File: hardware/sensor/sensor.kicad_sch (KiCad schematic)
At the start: 1 part, among them IC1 ATTINY202-SSN

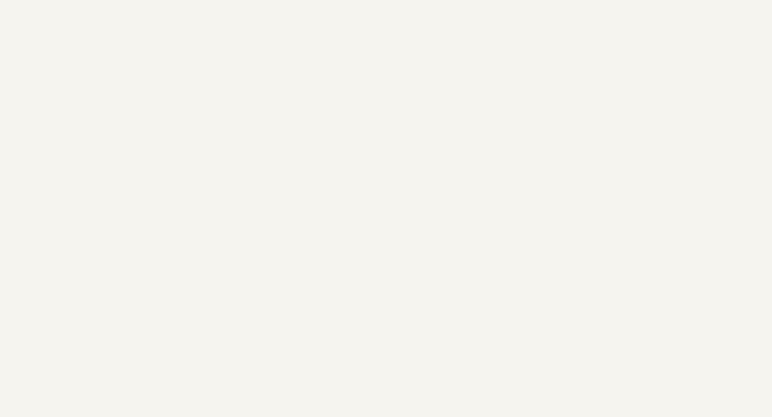
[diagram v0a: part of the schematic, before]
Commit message: EG-21 Added datasheets and the main ICs to KiCad project library, including symbol, footprint and 3D model.
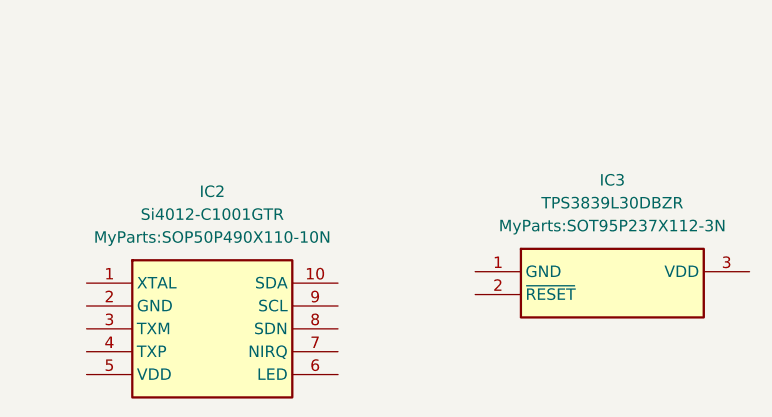
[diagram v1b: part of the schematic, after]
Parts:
- added IC2: Si4012-C1001GTR, MyParts:SOP50P490X110-10N, symbol Si4012-C1001GTR:Si4012-C1001GTR
- added IC3: TPS3839L30DBZR, MyParts:SOT95P237X112-3N, symbol TPS3839L30DBZR:TPS3839L30DBZR

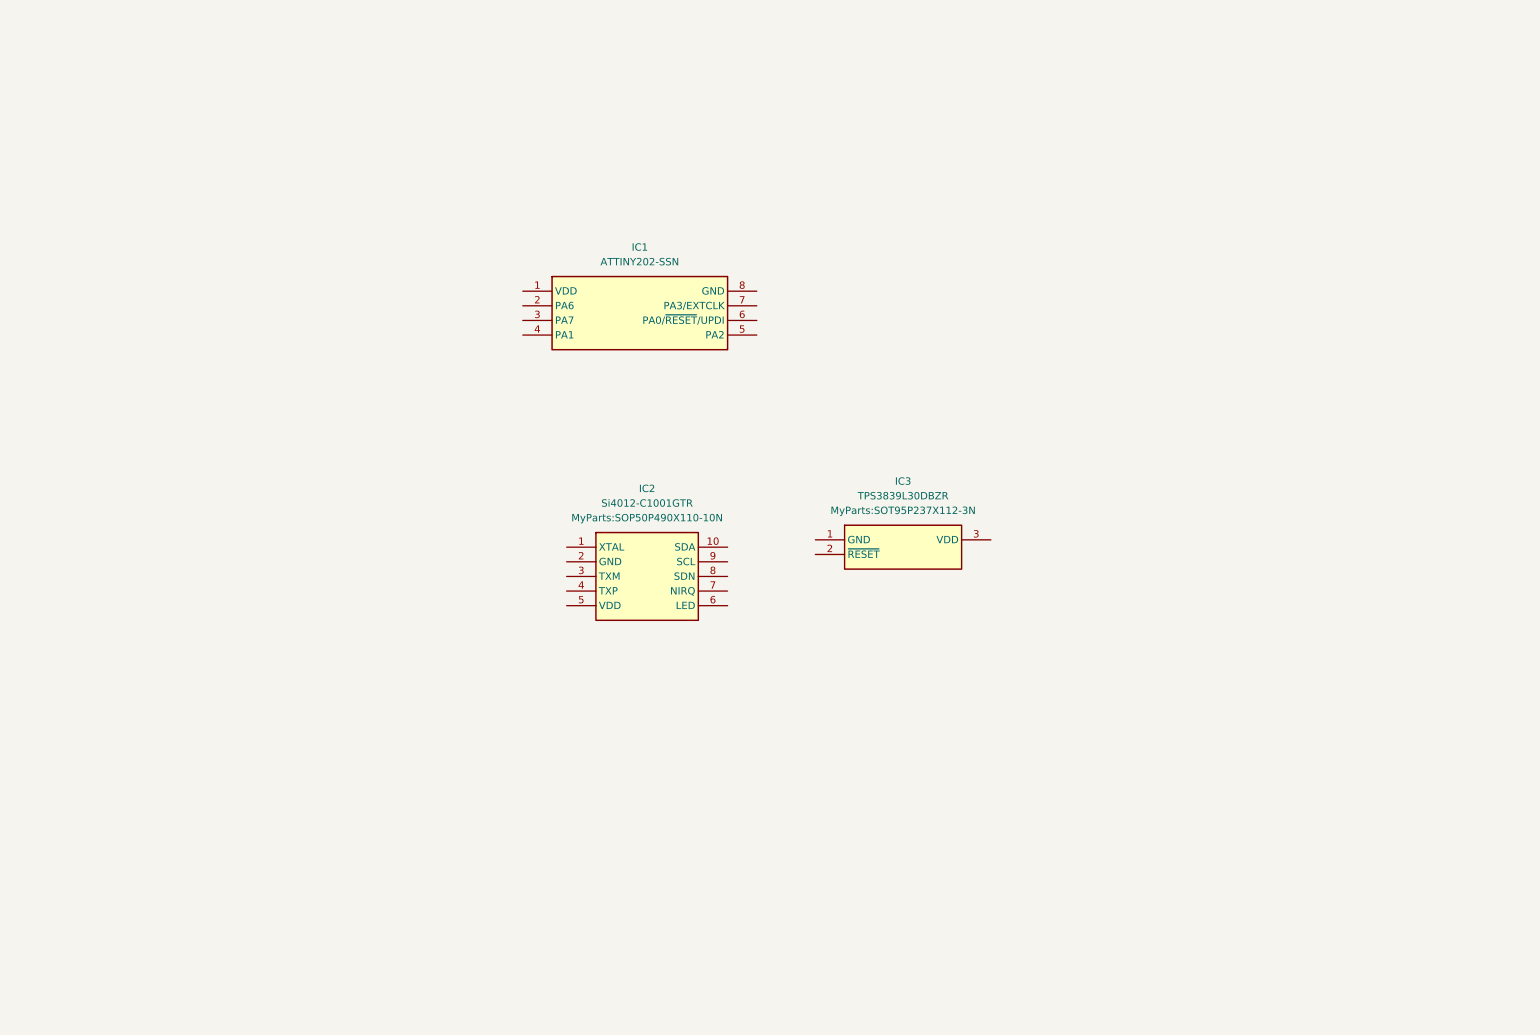
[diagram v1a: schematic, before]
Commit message: EG-21 Main components on schematic. Only missing I2C resistors, antenna, MCU RESET signal handling  and signals MCU<->Si4012.
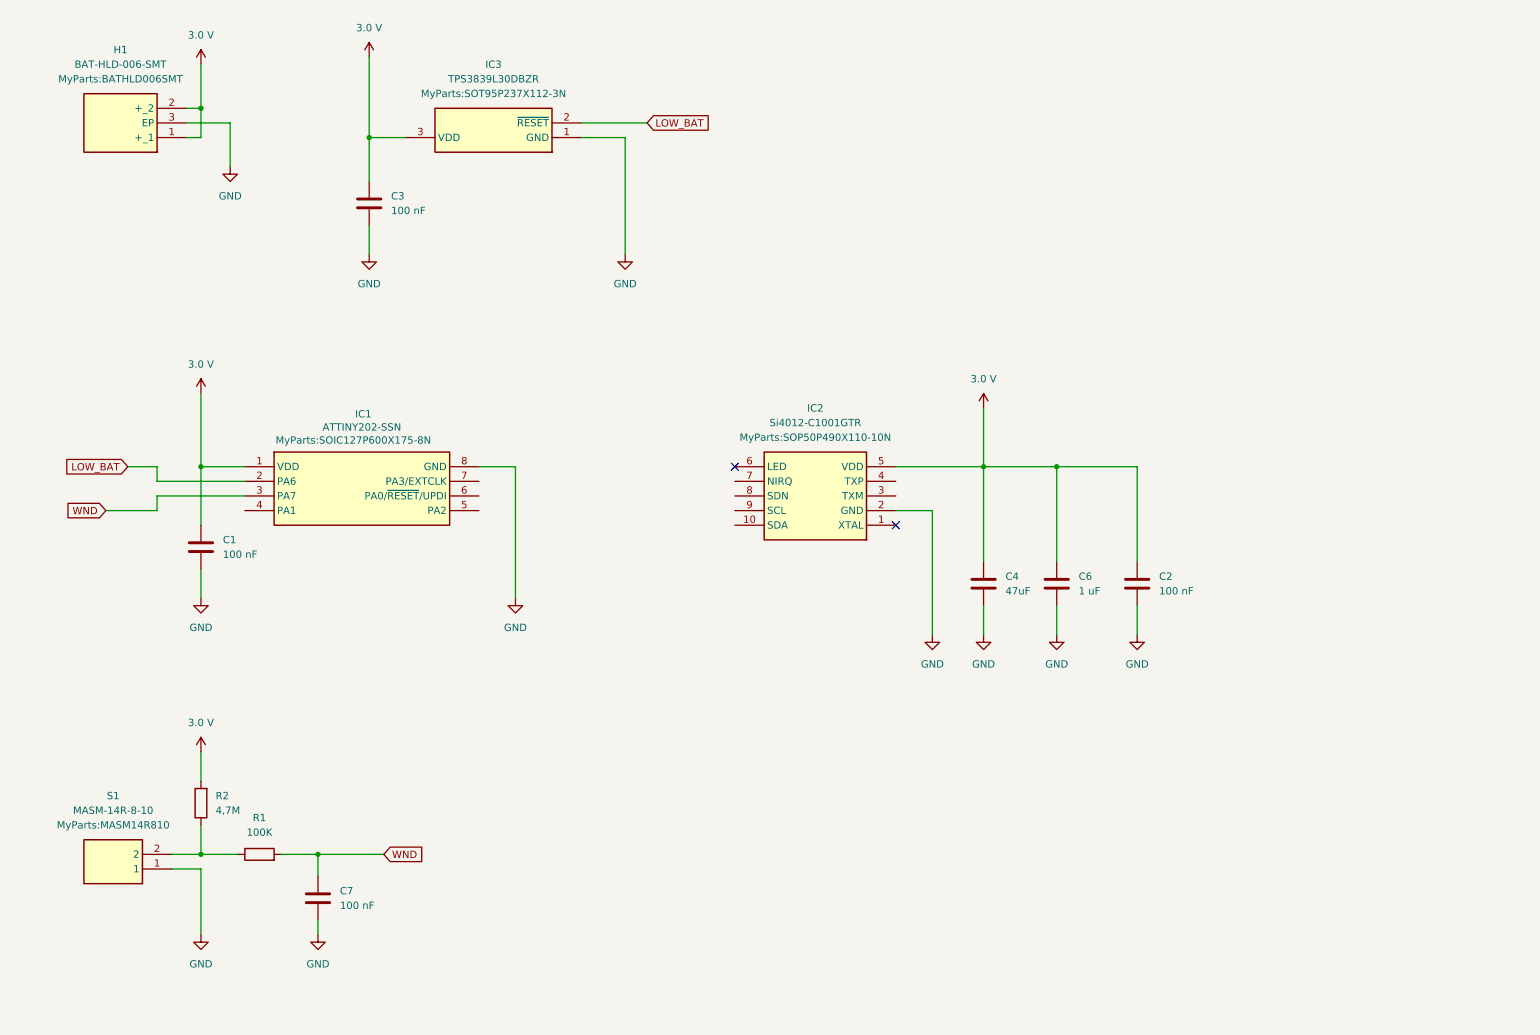
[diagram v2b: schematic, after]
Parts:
- added C1, C2, C3, C7: 100 nF, Capacitor_SMD:C_0603_1608Metric, symbol Device:C
- added C4: 47uF, symbol Device:C
- added C6: 1 uF, Capacitor_SMD:C_0603_1608Metric, symbol Device:C
- added H1: BAT-HLD-006-SMT, MyParts:BATHLD006SMT, symbol BAT-HLD-006-SMT:BAT-HLD-006-SMT
- added R1: 100K, Resistor_SMD:R_0201_0603Metric, symbol Device:R
- added R2: 4,7M, symbol Device:R
- added S1: MASM-14R-8-10, MyParts:MASM14R810, symbol MASM-14R-8-10:MASM-14R-8-10
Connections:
- net 3.0 V: now reaches IC1.1 (VDD)
- net 3.0 V: now also IC2.5 (VDD), IC3.3 (VDD), C1.1, C2.1, C3.1, C4.1, C6.1, H1.1 (+_1), H1.2 (+_2), R2.2
- net LOW_BAT: now reaches IC1.2 (PA6)
- net LOW_BAT: now also IC3.2 (~{RESET})
- net WND: now reaches IC1.3 (PA7)
- net WND: now also C7.1, R1.2
- net GND: now reaches IC1.8 (GND)
- net GND: now also IC2.2 (GND), IC3.1 (GND), C1.2, C2.2, C3.2, C4.2, C6.2, C7.2, H1.3 (EP), S1.1
- new net: R1.1, R2.1, S1.2
- no-connect marks 0 -> 2
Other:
- moved on the sheet: IC1, IC2, IC3

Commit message: EG-21 Added all components except the antenna balun and antenna footprint. Added the Si4012 antenna application note.
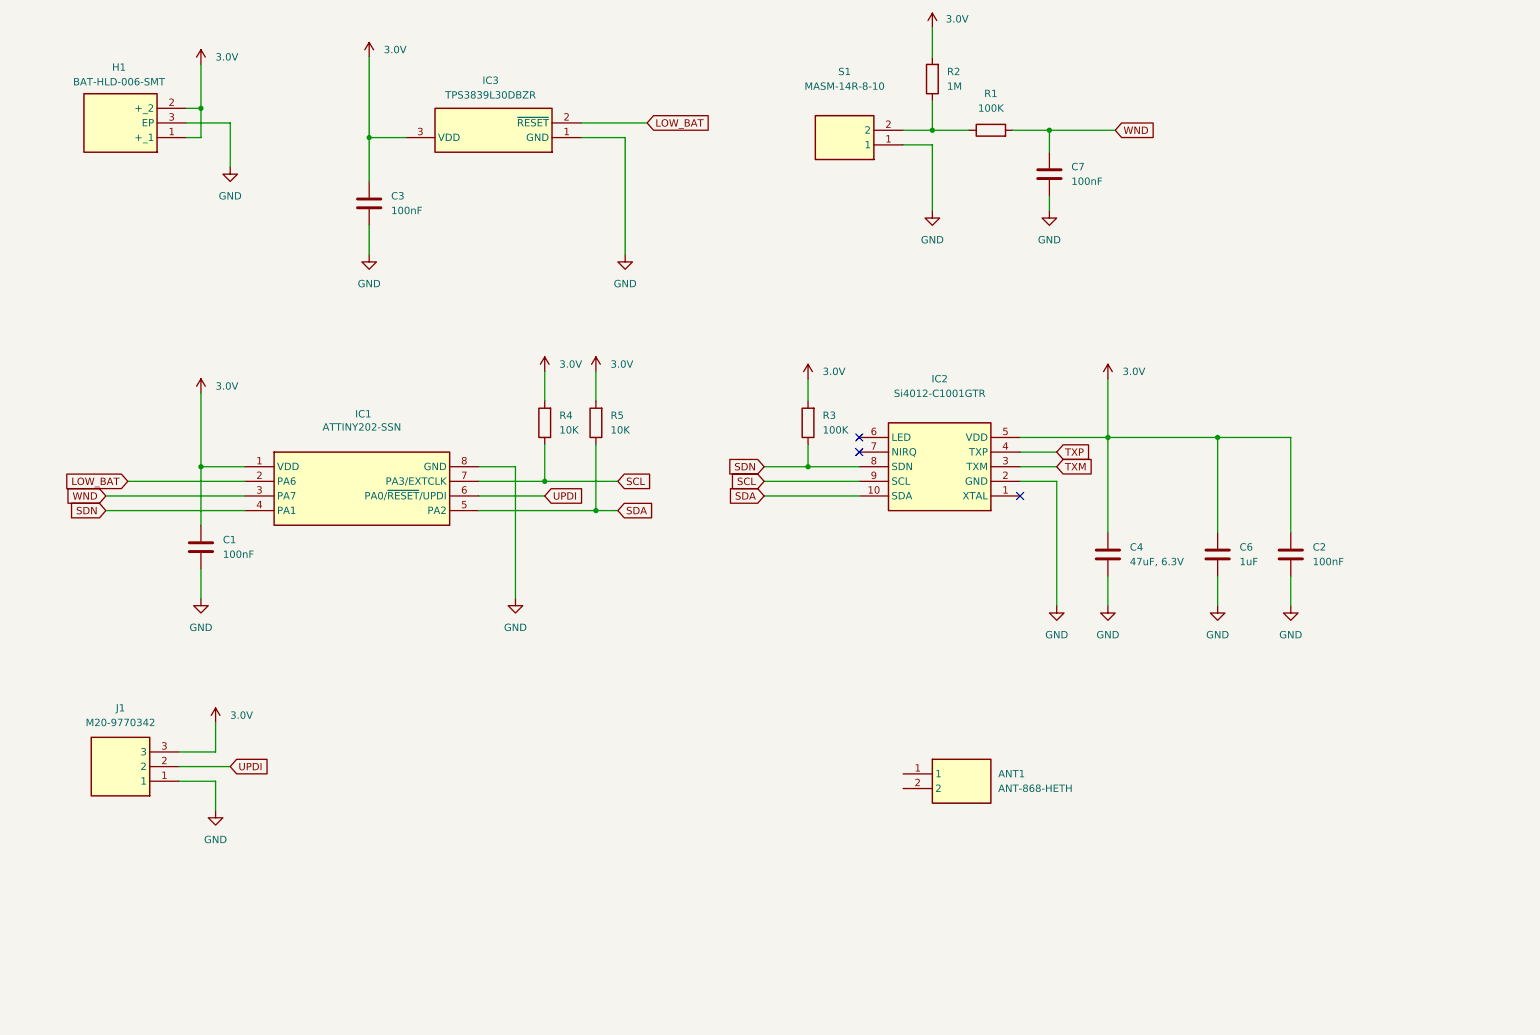
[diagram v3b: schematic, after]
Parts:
- added ANT1: ANT-868-HETH, ANT868HETH, symbol ANT-868-HESM:ANT-868-HETH
- added J1: M20-9770342, MyParts:HDRV3W66P0X254_1X3_762X254X855P, symbol M20-9770342:M20-9770342
- added R3: 100K, Resistor_SMD:R_0201_0603Metric, symbol Device:R
- added R4, R5: 10K, Resistor_SMD:R_0201_0603Metric, symbol Device:R
- C1, C2, C3, C7: value 100 nF -> 100nF
- C4: value 47uF -> 47uF, 6.3V; footprint (none) -> Capacitor_SMD:C_0805_2012Metric
- C6: value 1 uF -> 1uF
- R2: value 4,7M -> 1M
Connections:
- net GND: now also J1.1
- net SDN: now reaches IC1.4 (PA1)
- net SDN: now also IC2.8 (SDN), R3.1
- net SDA: now reaches IC1.5 (PA2)
- net SDA: now also IC2.10 (SDA), R5.1
- net UPDI: now reaches IC1.6 (PA0/~{RESET}/UPDI)
- net UPDI: now also J1.2
- net SCL: now reaches IC1.7 (PA3/EXTCLK)
- net SCL: now also IC2.9 (SCL), R4.1
- net TXM: now reaches IC2.3 (TXM)
- net TXP: now reaches IC2.4 (TXP)
- net 3.0 V renamed 3.0V
- net 3.0V: now also J1.3, R3.2, R4.2, R5.2
- no-connect marks 2 -> 3
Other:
- moved on the sheet: C2, C4, C6, C7, IC2, R1, R2, S1

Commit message: EG-21 Antenna and programming headers added. Missing the balun part and test points.
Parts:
- ANT1: footprint ANT868HETH -> MyParts:ANT-868-HESM
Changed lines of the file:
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@@
 			)
 		)
-		(property "Footprint" "ANT868HETH"
+		(property "Footprint" "MyParts:ANT-868-HESM"
 			(at 182.88 242.24 0)
 			(effects

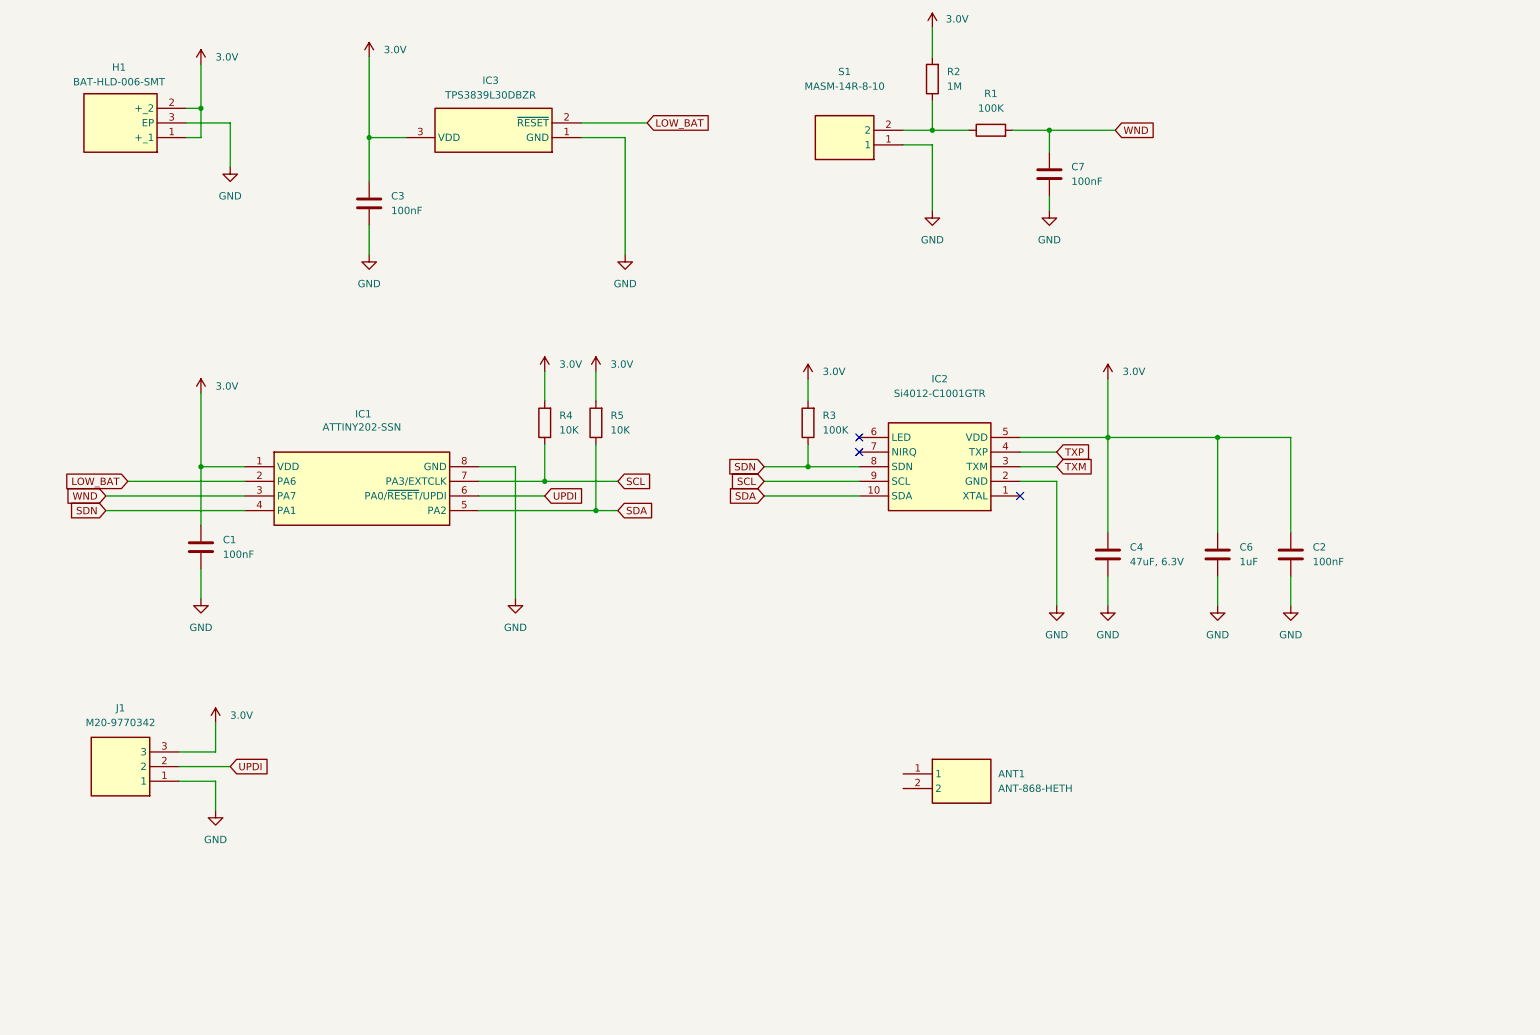
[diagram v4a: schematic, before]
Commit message: EG-21 Balun, pi-matching and antenna connected.
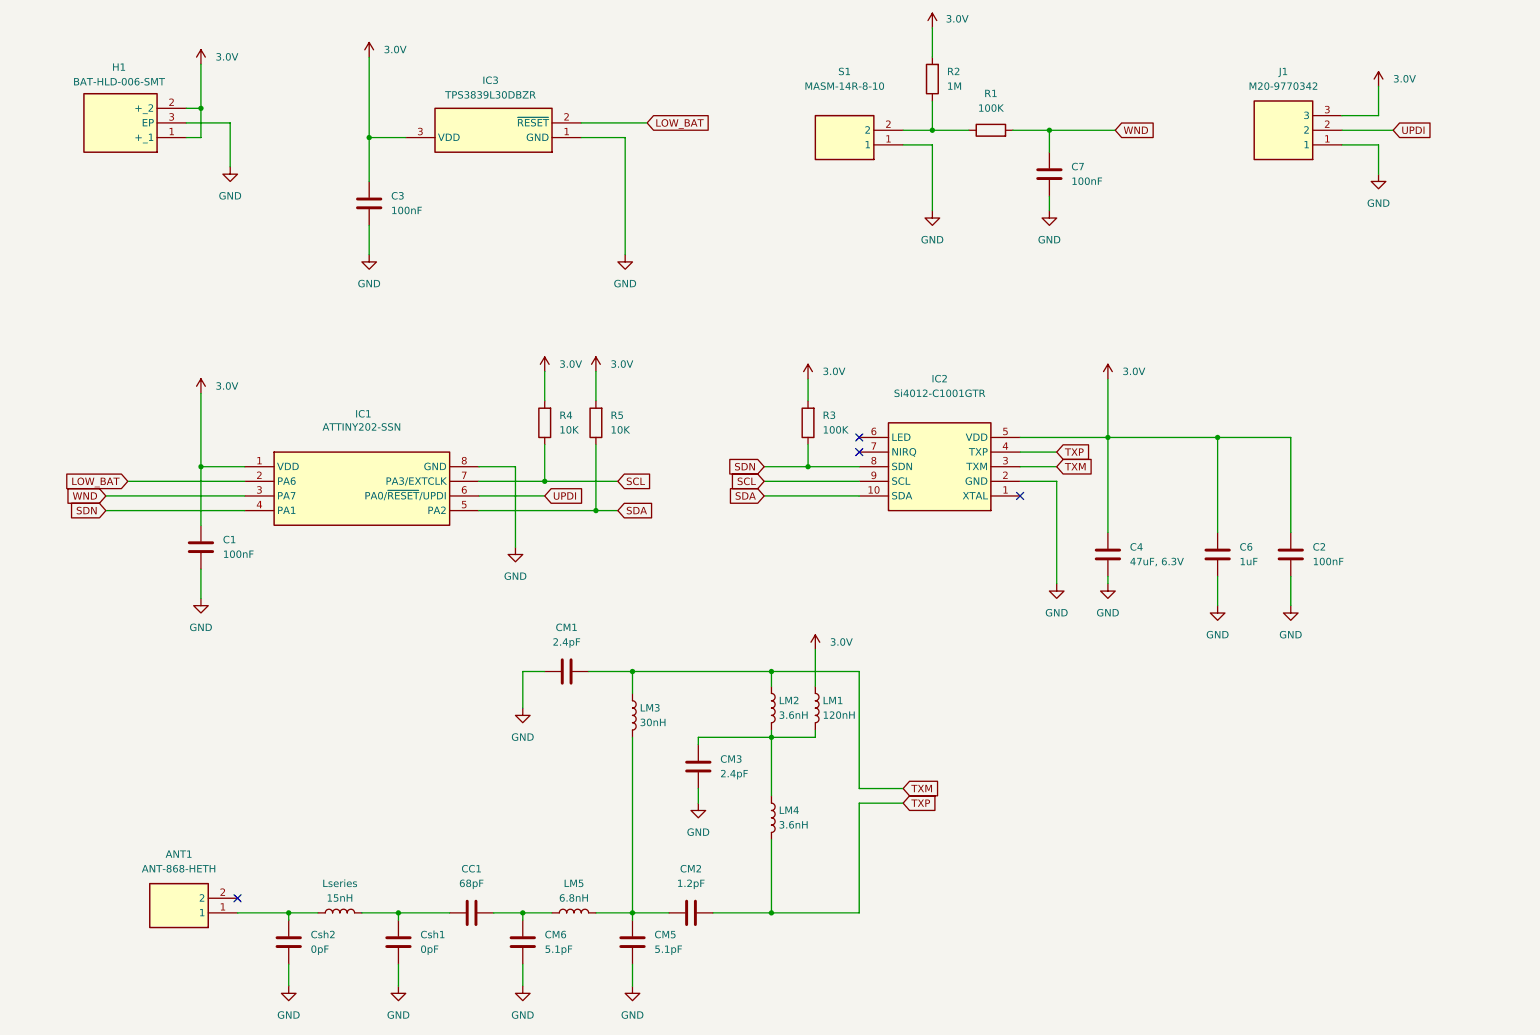
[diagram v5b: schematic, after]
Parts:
- added CC1: 68pF, Inductor_SMD:L_0402_1005Metric, symbol Device:C
- added CM1, CM3: 2.4pF, Inductor_SMD:L_0402_1005Metric, symbol Device:C
- added CM2: 1.2pF, Inductor_SMD:L_0402_1005Metric, symbol Device:C
- added CM5: 5.1pF, symbol Device:C
- added CM6: 5.1pF, Inductor_SMD:L_0402_1005Metric, symbol Device:C
- added Csh1, Csh2: 0pF, symbol Device:C
- added LM1: 120nH, Inductor_SMD:L_0603_1608Metric, symbol Device:L
- added LM2, LM4: 3.6nH, Inductor_SMD:L_0402_1005Metric, symbol Device:L
- added LM3: 30nH, Inductor_SMD:L_0402_1005Metric, symbol Device:L
- added LM5: 6.8nH, Inductor_SMD:L_0402_1005Metric, symbol Device:L
- added Lseries: 15nH, Inductor_SMD:L_0402_1005Metric, symbol Device:L
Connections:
- net 3.0V: now also LM1.1
- net GND: now also CM1.2, CM3.2, CM5.2, CM6.2, Csh1.2, Csh2.2
- net TXM: now also CM1.1, LM2.1, LM3.1
- net TXP: now also CM2.2, LM4.2
- net at ANT1.1: now also Csh2.1, Lseries.1
- new net: CM2.1, CM5.1, LM3.2, LM5.2
- new net: CC1.2, CM6.1, LM5.1
- new net: CM3.1, LM1.2, LM2.2, LM4.1
- new net: CC1.1, Csh1.1, Lseries.2
- no-connect marks 3 -> 4
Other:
- moved on the sheet: ANT1, J1
